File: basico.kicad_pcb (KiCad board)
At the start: 2 copper layers, 85.9 x 99.9 mm, 8 parts, among them P1 Power, P2 Analog, P3 Analog, P4 Digital, P5 PWM, P6 PWM, P7 Communication

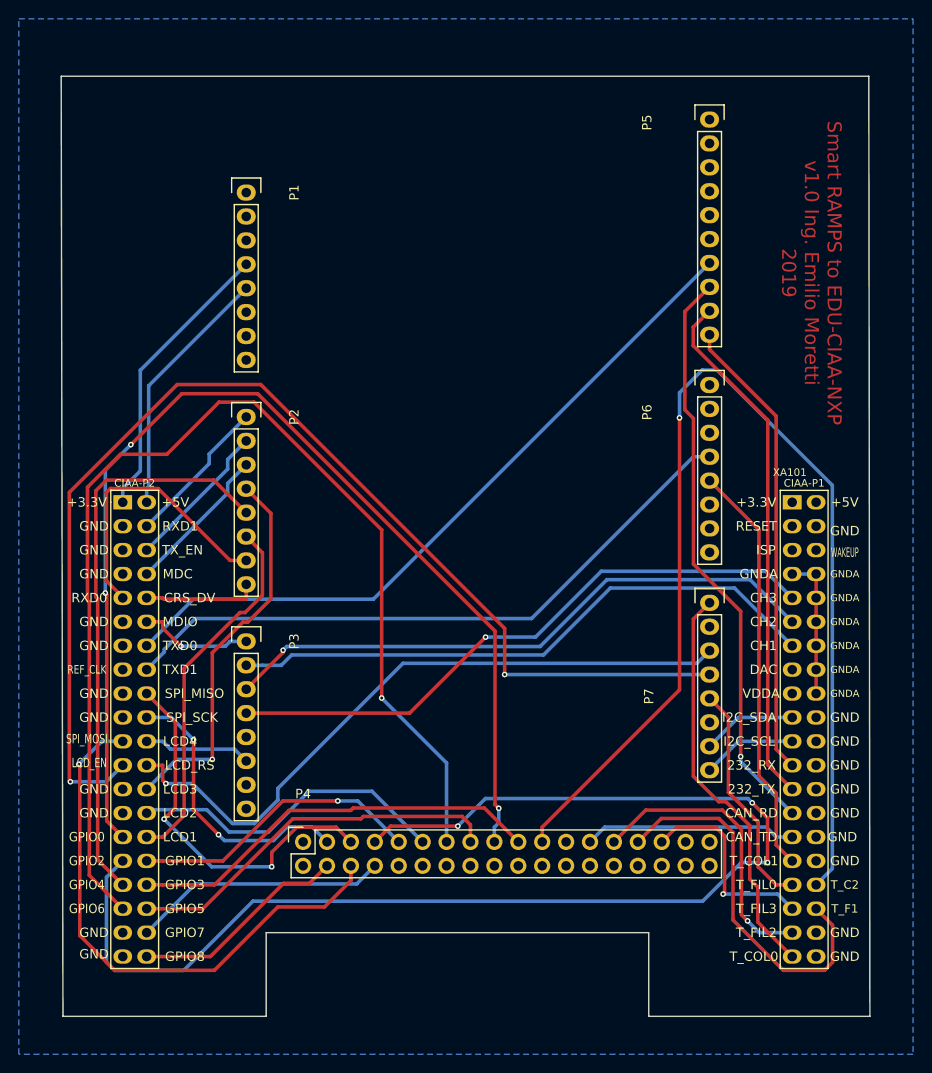
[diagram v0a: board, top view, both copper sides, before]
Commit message: Agregar led y re-ruteo
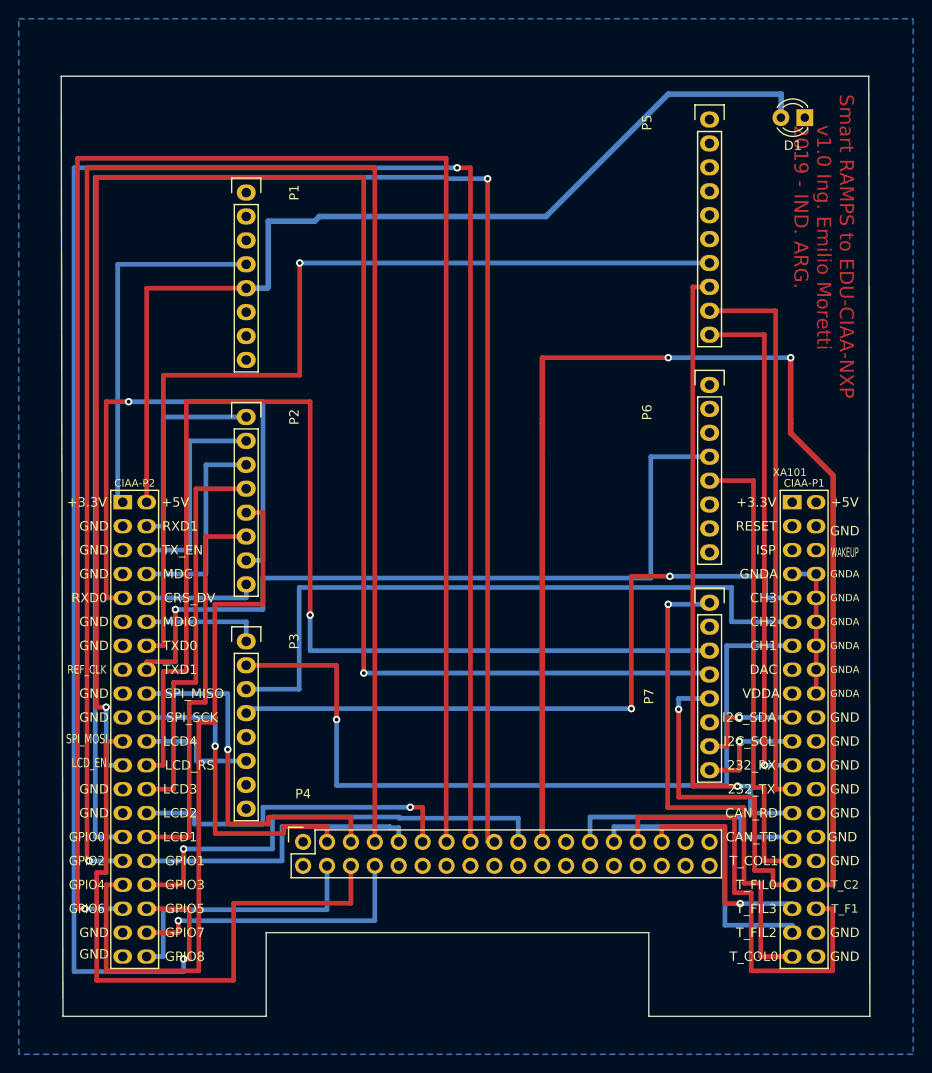
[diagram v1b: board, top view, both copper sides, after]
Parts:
- added D1: LED, LED_THT:LED_D3.0mm, F.Cu at (138.5, 45.5)
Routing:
- net /Ar_40: track 40.6 -> 222.5 mm, vias 0 -> 2
- net +5V: track 27.1 -> 105.5 mm
- net /Ar_42: track 123.0 -> 196.4 mm
- net /Ar_38: track 117.7 -> 186.0 mm, vias 3 -> 1
- net /Ar_17: track 125.5 -> 183.2 mm
- net /Ar_16: track 71.6 -> 124.9 mm
- net /Ar_48: track 136.0 -> 179.6 mm, vias 3 -> 1
- net /Ar_A6: track 30.1 -> 57.9 mm, vias 0 -> 1
- net /Ar_11: track 76.6 -> 100.5 mm, vias 0 -> 1
- net /Ar_A9: track 63.9 -> 85.6 mm, vias 0 -> 1
- net /Ar_34: track 119.2 -> 137.6 mm, vias 1 -> 2
- net /Ar_A4: track 60.9 -> 78.0 mm
- net /Ar_4: track 69.3 -> 82.4 mm, vias 0 -> 1
- net /Ar_14: track 43.1 -> 55.3 mm, vias 0 -> 1
- net /Ar_18: track 24.4 -> 35.2 mm, vias 0 -> 1
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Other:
- net class Default: trace_width 0.381 -> 0.5; via_dia 0.6 -> 0.8; via_drill 0.4 -> 0.6
- board text added: "Diseño doble faz. Sin requerimientos especiales."
- board text added: "Poncho Smart RAMPS para EDU-CIAA-NXP https://github.com/dc740/smart-ramps-to-edu-ciaa"
- board text added: "Smart RAMPS to EDU-CIAA-NXP v1.0 Ing. Emilio Moretti 2019 - IND. ARG."
- board text removed: "Diseño simple faz. Sin requerimientos especiales."
- board text removed: "PONCHO BASICO http://www.proyecto-ciaa.com.ar/"
- board text removed: "Smart RAMPS to EDU-CIAA-NXP v1.0 Ing. Emilio Moretti 2019"

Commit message: Fix led
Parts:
- added R1: 10k, Resistor_THT:R_Axial_DIN0204_L3.6mm_D1.6mm_P5.08mm_Horizontal, F.Cu at (133.5, 46.0)
- moved D1 0.71 mm to (138.0, 46.0), turned to 90 degrees
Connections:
- D1 pad 1: GND -> Net-(D1-Pad1)
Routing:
- net Net-(D1-Pad1): track 0.00 -> 4.50 mm
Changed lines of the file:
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@@
     (thickness 1.6)
     (drawings 26)
-    (tracks 291)
+    (tracks 290)
     (zones 0)
-    (modules 9)
-    (nets 47)
+    (modules 10)
+    (nets 48)
   )
   (page A4)
@@
   )
   (setup
-    (last_trace_width 0.6)
+    (last_trace_width 0.5)
     (user_trace_width 0.508)
     (user_trace_width 0.6)
@@
   (net 45 /Ar_A10)
   (net 46 /Ar_A9)
+  (net 47 "Net-(D1-Pad1)")
   (net_class Default "This is the default net class."
     (clearance 0.51)
@@
     (add_net GND)
     (add_net GNDA)
+    (add_net "Net-(D1-Pad1)")
+  )
+  (module Resistor_THT:R_Axial_DIN0204_L3.6mm_D1.6mm_P5.08mm_Horizontal (layer F.Cu)
+    (at 133.5 46 270)
+    (descr "Resistor, Axial_DIN0204 series, Axial, Horizontal, pin pitch=5.08mm, 0.167W, length*diameter=3.6*1.6mm^2, http://cdn-reichelt.de/documents/datenblatt/B400/1_4W%23YAG.pdf")
+    (tags "Resistor Axial_DIN0204 series Axial Horizontal pin pitch 5.08mm 0.167W length 3.6mm diameter 1.6mm")
+    (fp_text reference R1 (at 2.54 -1.92 90) (layer F.SilkS)
+      (effects (font (size 1 1) (thickness 0.15)))
+    )
+    (fp_text value 10k (at 2.54 1.92 90) (layer F.Fab)
+      (effects (font (size 1 1) (thickness 0.15)))
+    )
+    (fp_text user %R (at 2.54 0 90) (layer F.Fab)
+      (effects (font (size 0.72 0.72) (thickness 0.108)))
+    )
+    (fp_line (start 6.03 -1.05) (end -0.95 -1.05) (layer F.CrtYd) (width 0.05))
+    (fp_line (start 6.03 1.05) (end 6.03 -1.05) (layer F.CrtYd) (width 0.05))
+    (fp_line (start -0.95 1.05) (end 6.03 1.05) (layer F.CrtYd) (width 0.05))
+    (fp_line (start -0.95 -1.05) (end -0.95 1.05) (layer F.CrtYd) (width 0.05))
+    (fp_line (start 0.62 0.92) (end 4.46 0.92) (layer F.SilkS) (width 0.12))
+    (fp_line (start 0.62 -0.92) (end 4.46 -0.92) (layer F.SilkS) (width 0.12))
+    (fp_line (start 5.08 0) (end 4.34 0) (layer F.Fab) (width 0.1))
+    (fp_line (start 0 0) (end 0.74 0) (layer F.Fab) (width 0.1))
+    (fp_line (start 4.34 -0.8) (end 0.74 -0.8) (layer F.Fab) (width 0.1))
+    (fp_line (start 4.34 0.8) (end 4.34 -0.8) (layer F.Fab) (width 0.1))
+    (fp_line (start 0.74 0.8) (end 4.34 0.8) (layer F.Fab) (width 0.1))
+    (fp_line (start 0.74 -0.8) (end 0.74 0.8) (layer F.Fab) (width 0.1))
+    (pad 2 thru_hole oval (at 5.08 0 270) (size 1.4 1.4) (drill 0.7) (layers *.Cu *.Mask)
+      (net 2 GND))
+    (pad 1 thru_hole circle (at 0 0 270) (size 1.4 1.4) (drill 0.7) (layers *.Cu *.Mask)
+      (net 47 "Net-(D1-Pad1)"))
+    (model ${KISYS3DMOD}/Resistor_THT.3dshapes/R_Axial_DIN0204_L3.6mm_D1.6mm_P5.08mm_Horizontal.wrl
+      (at (xyz 0 0 0))
+      (scale (xyz 1 1 1))
+      (rotate (xyz 0 0 0))
+    )
   )
   (module LED_THT:LED_D3.0mm (layer F.Cu)
-    (at 138.5 45.5 180)
+    (at 138 46 90)
     (descr "LED, diameter 3.0mm, 2 pins")
     (tags "LED diameter 3.0mm 2 pins")
-    (fp_text reference D1 (at 1.27 -2.96) (layer F.SilkS)
-      (effects (font (size 1 1) (thickness 0.15)))
-    )
-    (fp_text value LED (at 1.27 2.96) (layer F.Fab)
+    (fp_text reference D1 (at 1.27 -2.96 90) (layer F.SilkS)
+      (effects (font (size 1 1) (thickness 0.15)))
+    )
+    (fp_text value LED (at 1.27 2.96 90) (layer F.Fab)
       (effects (font (size 1 1) (thickness 0.15)))
     )
@@
     (fp_arc (start 1.27 0) (end -0.29 -1.235516) (angle 108.8) (layer F.SilkS) (width 0.12))
     (fp_arc (start 1.27 0) (end -0.23 -1.16619) (angle 284.3) (layer F.Fab) (width 0.1))
-    (pad 2 thru_hole circle (at 2.54 0 180) (size 1.8 1.8) (drill 0.9) (layers *.Cu *.Mask)
+    (pad 2 thru_hole circle (at 2.54 0 90) (size 1.8 1.8) (drill 0.9) (layers *.Cu *.Mask)
       (net 1 +5V))
-    (pad 1 thru_hole rect (at 0 0 180) (size 1.8 1.8) (drill 0.9) (layers *.Cu *.Mask)
-      (net 2 GND))
+    (pad 1 thru_hole rect (at 0 0 90) (size 1.8 1.8) (drill 0.9) (layers *.Cu *.Mask)
+      (net 47 "Net-(D1-Pad1)"))
     (model ${KISYS3DMOD}/LED_THT.3dshapes/LED_D3.0mm.wrl
       (at (xyz 0 0 0))
@@
   (segment (start 79.16 63.62) (end 68.58 63.62) (width 0.5) (layer F.Cu) (net 1) (status 10))
   (segment (start 68.58 63.62) (end 68.58 86.36) (width 0.5) (layer F.Cu) (net 1) (status 20))
-  (segment (start 136 44.187208) (end 135.96 44.227208) (width 0.6) (layer B.Cu) (net 1))
-  (segment (start 136 43) (end 136 44.187208) (width 0.6) (layer B.Cu) (net 1))
+  (segment (start 79.16 63.62) (end 79.3124 63.62) (width 0.6) (layer B.Cu) (net 1))
+  (segment (start 137.54 43) (end 138 43.46) (width 0.6) (layer B.Cu) (net 1))
+  (segment (start 124 43) (end 137.54 43) (width 0.6) (layer B.Cu) (net 1))
   (segment (start 86.9324 56) (end 111 56) (width 0.6) (layer B.Cu) (net 1))
-  (segment (start 79.16 63.62) (end 79.3124 63.62) (width 0.6) (layer B.Cu) (net 1))
+  (segment (start 79.16 63.62) (end 81.38 63.62) (width 0.6) (layer B.Cu) (net 1))
   (segment (start 111 56) (end 124 43) (width 0.6) (layer B.Cu) (net 1))
-  (segment (start 135.96 44.227208) (end 135.96 45.5) (width 0.6) (layer B.Cu) (net 1))
-  (segment (start 124 43) (end 136 43) (width 0.6) (layer B.Cu) (net 1))
-  (segment (start 79.16 63.62) (end 81.38 63.62) (width 0.6) (layer B.Cu) (net 1))
   (segment (start 81.38 63.62) (end 81.5 63.5) (width 0.6) (layer B.Cu) (net 1))
   (segment (start 81.5 63.5) (end 81.5 56.5) (width 0.6) (layer B.Cu) (net 1))
@@
   (segment (start 88.758 103.68) (end 79.16 103.68) (width 0.5) (layer F.Cu) (net 46) (status 20))
   (via (at 88.758 109.4415) (size 0.8) (layers F.Cu B.Cu) (net 46))
+  (segment (start 133.5 46) (end 138 46) (width 0.5) (layer F.Cu) (net 47))
   (zone (net 2) (net_name GND) (layer B.Cu) (hatch edge 0.508)
     (connect_pads (clearance 0.8))

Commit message: Connect analog ground
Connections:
- XA101 pad 10: GNDA -> GND
- XA101 pad 12: GNDA -> GND
- XA101 pad 14: GNDA -> GND
- XA101 pad 16: GNDA -> GND
- XA101 pad 18: GNDA -> GND
- XA101 pad 7: GNDA -> GND
- XA101 pad 8: GNDA -> GND
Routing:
- net GNDA: track 15.2 -> 0.00 mm
- net GND: track 0.00 -> 15.2 mm

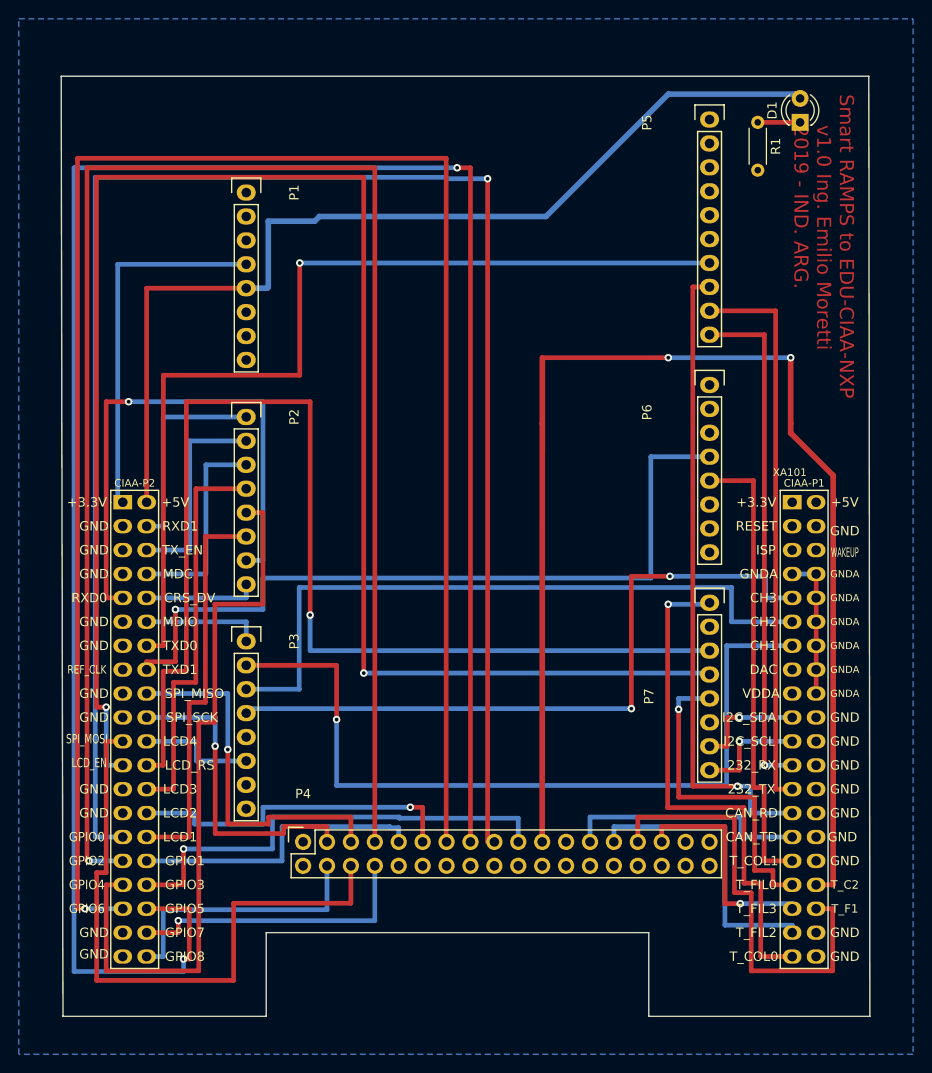
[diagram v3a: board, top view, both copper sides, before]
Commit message: Add fixes and correct tracks
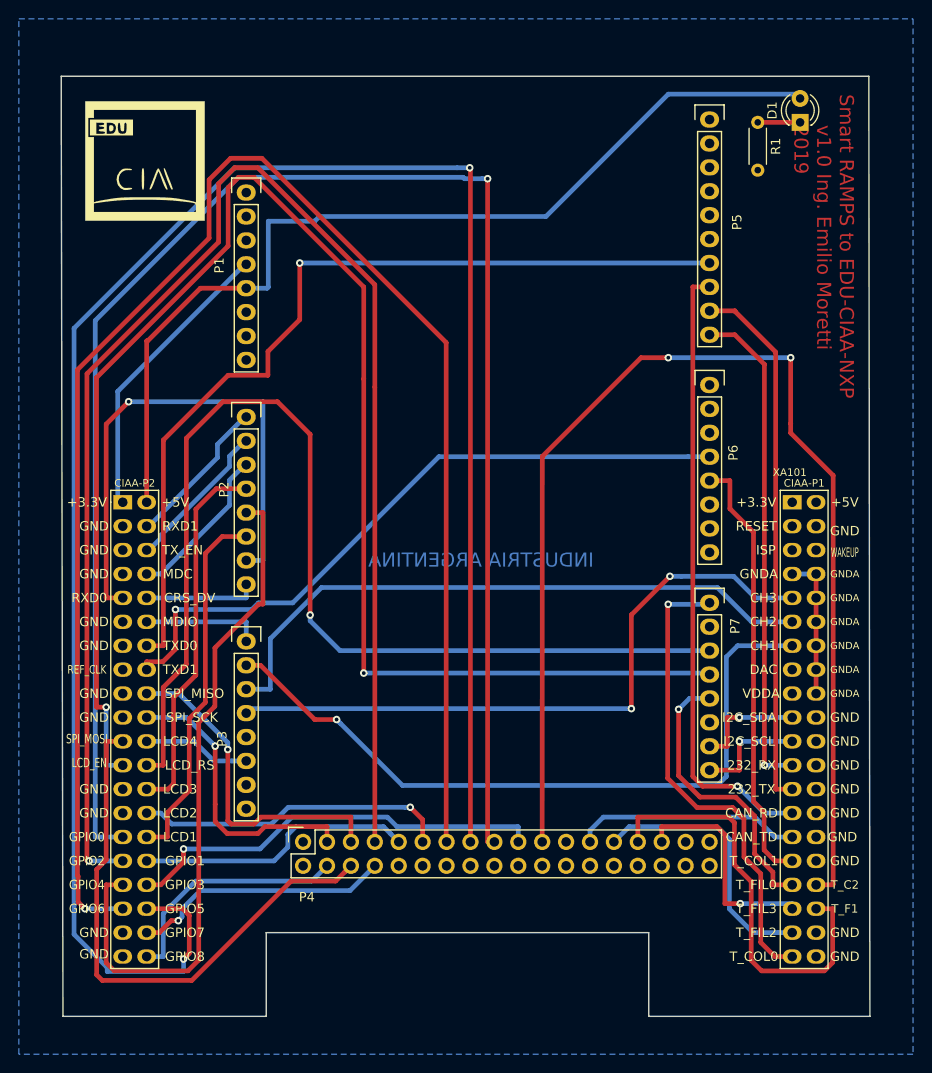
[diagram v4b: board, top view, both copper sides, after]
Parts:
- added G***: Logo_EDU-CIAA, footprint:Logo_EDU-CIAA, F.Cu at (68.4, 50.1)
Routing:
- net /Ar_42: track 196.4 -> 174.9 mm
- net /Ar_48: track 179.6 -> 163.2 mm
- net /Ar_17: track 183.2 -> 167.5 mm
- net /Ar_40: track 222.5 -> 209.6 mm
- net /Ar_4: track 82.4 -> 72.1 mm
- net /Ar_38: track 186.0 -> 177.0 mm
- net /Ar_A9: track 85.6 -> 76.9 mm
- net /Ar_51: track 67.3 -> 59.3 mm
- net +3.3VP: track 39.5 -> 31.6 mm
- net /Ar_16: track 124.9 -> 117.3 mm
- net /Ar_34: track 137.6 -> 131.4 mm
- net /Ar_11: track 100.5 -> 94.5 mm
- net /Ar_A0: track 22.2 -> 16.2 mm
- net /Ar_A1: track 22.2 -> 16.2 mm
- net /Ar_A10: track 72.4 -> 67.1 mm
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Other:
- board text added: "Diseño doble faz. Sin requerimientos especiales. Track 0,5mm Via 0,80/0,40 Grid:0,1mm Margen:0,5mm"
- board text added: "INDUSTRIA ARGENTINA"
- board text added: "Smart RAMPS to EDU-CIAA-NXP v1.0 Ing. Emilio Moretti 2019"
- board text removed: "Diseño doble faz. Sin requerimientos especiales."
- board text removed: "Smart RAMPS to EDU-CIAA-NXP v1.0 Ing. Emilio Moretti 2019 - IND. ARG."
